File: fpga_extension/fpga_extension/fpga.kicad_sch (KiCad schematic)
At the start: 50 parts, among them U2 t20f169

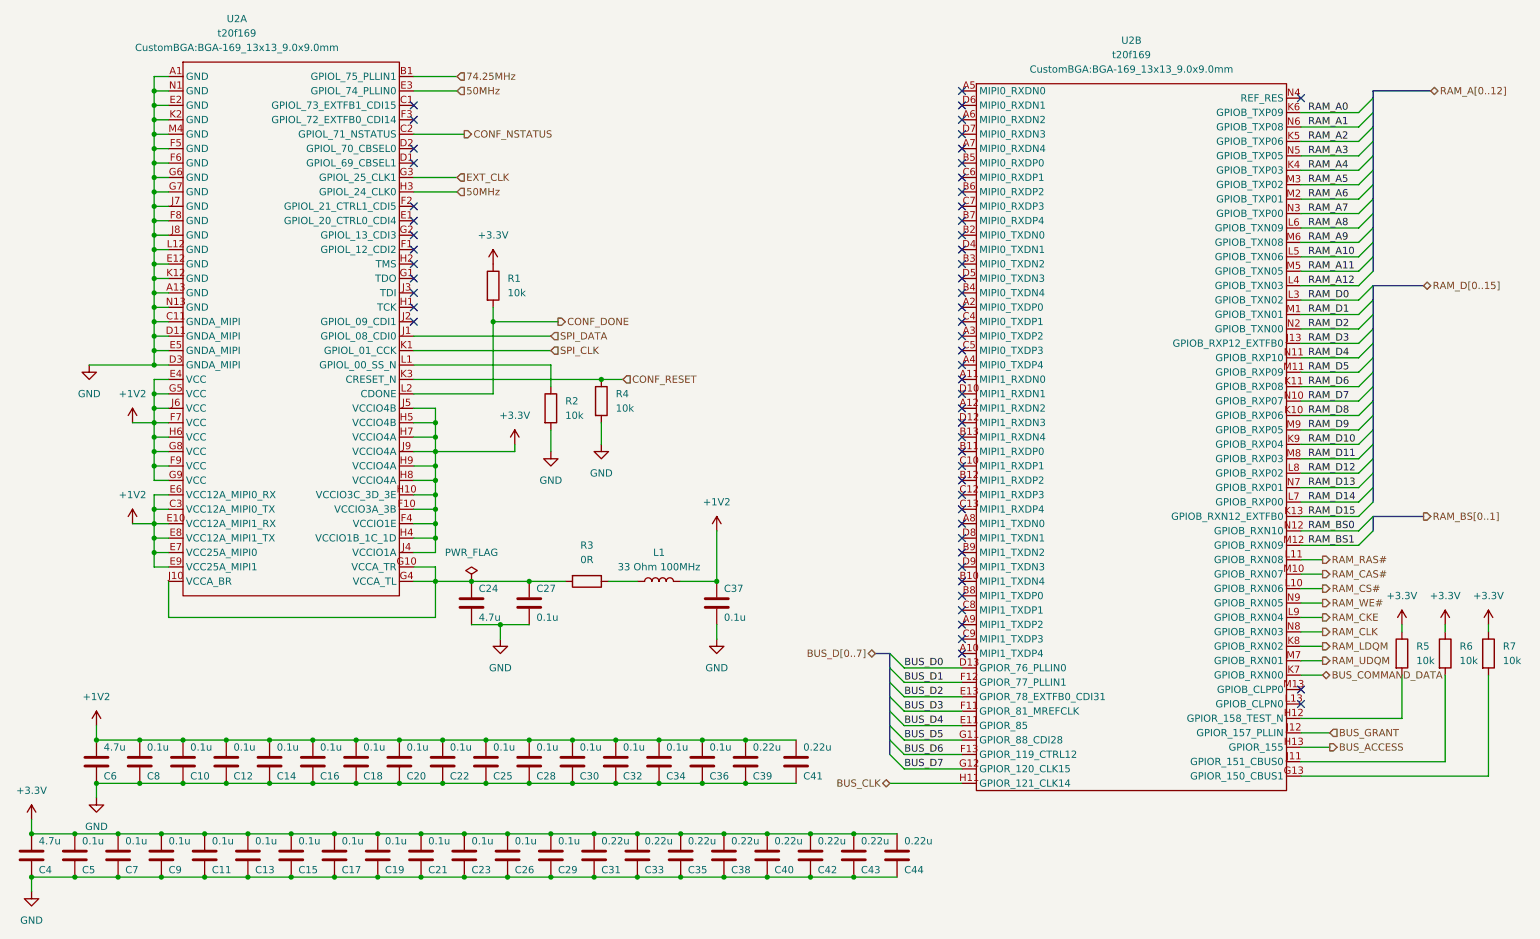
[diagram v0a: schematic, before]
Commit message: working on new version of fpga extension with Lattice FPGA
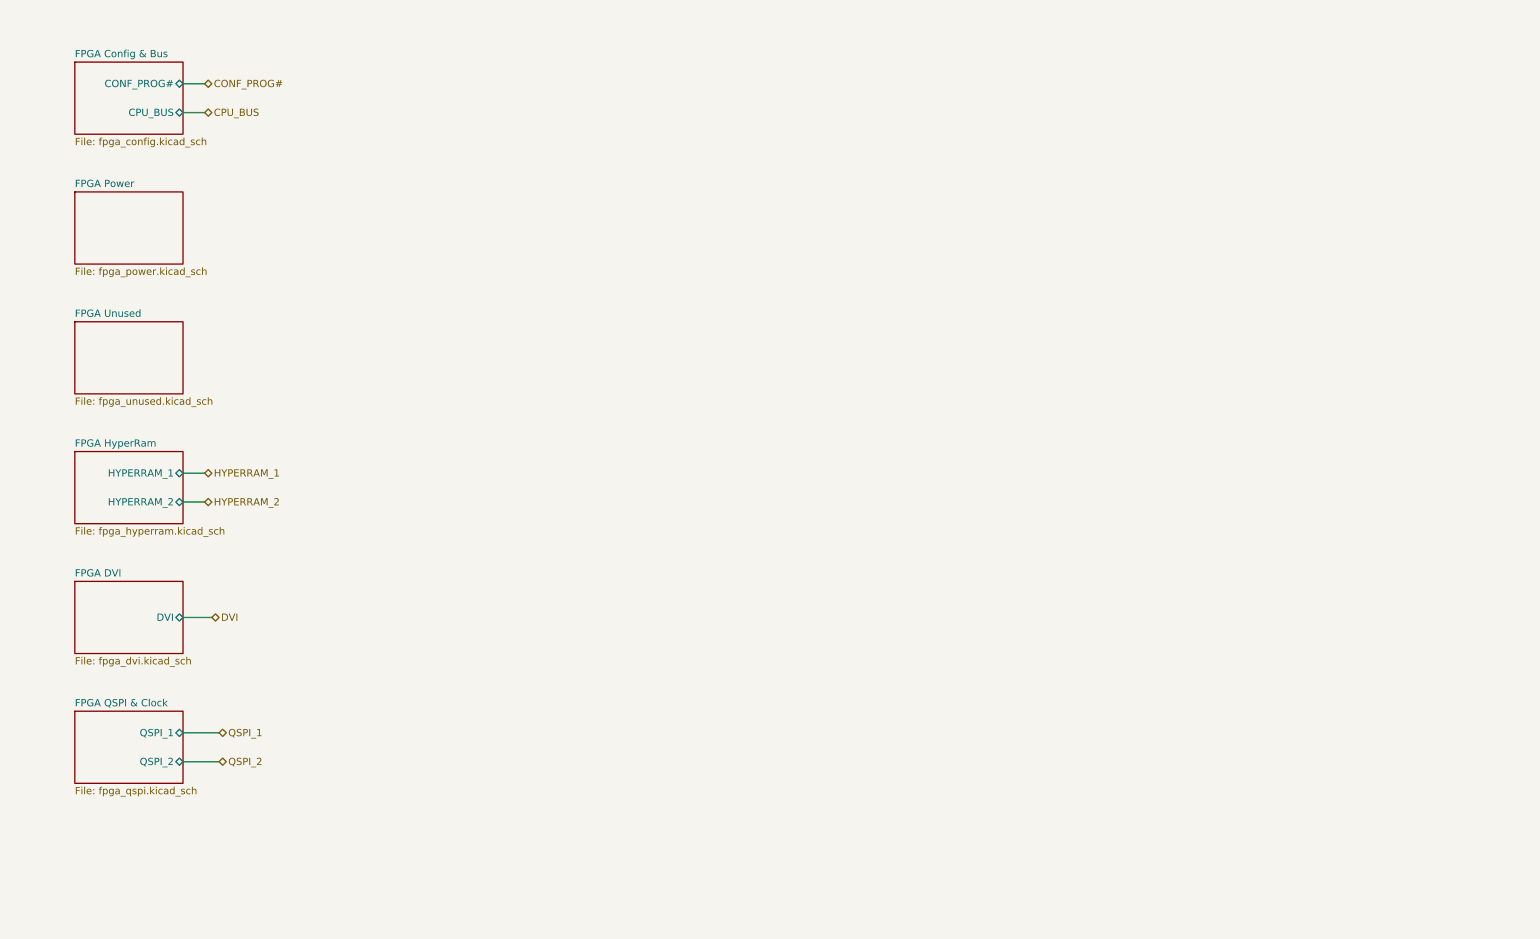
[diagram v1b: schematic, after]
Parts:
- removed C10, C11, C12, C13, C14, C15, C16, C17, C18, C19, C20, C21, C22, C23, C25, C26, C27, C28, C29, C30, C32, C34, C36, C37, C5, C7, C8, C9: 0.1u, Capacitor_SMD:C_0201_0603Metric_Pad0.64x0.40mm_HandSolder, symbol Device:C
- removed C24: 4.7u, Capacitor_SMD:C_0201_0603Metric_Pad0.64x0.40mm_HandSolder, symbol Device:C
- removed C31, C33, C35, C38, C39, C40, C41, C42, C43, C44: 0.22u, Capacitor_SMD:C_0201_0603Metric_Pad0.64x0.40mm_HandSolder, symbol Device:C
- removed C4, C6: 4.7u, Capacitor_SMD:C_0402_1005Metric_Pad0.74x0.62mm_HandSolder, symbol Device:C
- removed L1: 33 Ohm 100MHz, Inductor_SMD:L_0402_1005Metric_Pad0.77x0.64mm_HandSolder, symbol Device:L
- removed R1, R2, R4, R5, R6, R7: 10k, Resistor_SMD:R_0603_1608Metric_Pad0.98x0.95mm_HandSolder, symbol Device:R
- removed R3: 0R, Resistor_SMD:R_0201_0603Metric_Pad0.64x0.40mm_HandSolder, symbol Device:R
- removed U2: t20f169, CustomBGA:BGA-169_13x13_9.0x9.0mm, symbol FPGA_Efinix:t20f169
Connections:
- no-connect marks 56 -> 0
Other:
- added sheet FPGA Config & Bus (fpga_config.kicad_sch)
- added sheet FPGA DVI (fpga_dvi.kicad_sch)
- added sheet FPGA HyperRam (fpga_hyperram.kicad_sch)
- added sheet FPGA Power (fpga_power.kicad_sch)
- added sheet FPGA QSPI & Clock (fpga_qspi.kicad_sch)
- added sheet FPGA Unused (fpga_unused.kicad_sch)

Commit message: refactored mainboard schematic
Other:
- sheet FPGA Config & Bus renamed FPGA Config, Bus & Clock
- sheet FPGA HyperRam renamed FPGA RAM
- removed sheet FPGA DVI
- sheet FPGA Config, Bus & Clock ports: added BUS{IO[0...7] CS#[0..1] INT RE# CLK RWDS}, JTAG{TDO TCK TDI TMS}; removed CONF_PROG#, CPU_BUS
- sheet FPGA QSPI & Clock ports: added QSPI1{CE# SCLK IO[0...3]}, QSPI2{CE# SCLK IO[0...3]}; removed QSPI_1, QSPI_2
- sheet FPGA RAM ports: added none; removed HYPERRAM_1, HYPERRAM_2
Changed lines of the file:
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@@
 (kicad_sch (version 20221004) (generator eeschema)
   (paper "A4")
-  (wire (pts (xy 44.45 29.21) (xy 48.26 29.21))
-    (stroke (width 0) (type default))
-  )
-  (wire (pts (xy 44.45 143.51) (xy 50.8 143.51))
-    (stroke (width 0) (type default))
-  )
-  (wire (pts (xy 44.45 148.59) (xy 50.8 148.59))
-    (stroke (width 0) (type default))
-  )
-  (wire (pts (xy 44.45 102.87) (xy 48.26 102.87))
-    (stroke (width 0) (type default))
-  )
-  (wire (pts (xy 44.45 34.29) (xy 48.26 34.29))
-    (stroke (width 0) (type default))
-  )
-  (wire (pts (xy 44.45 123.19) (xy 49.53 123.19))
-    (stroke (width 0) (type default))
-  )
-  (wire (pts (xy 44.45 97.79) (xy 48.26 97.79))
-    (stroke (width 0) (type default))
-  )
-  (hierarchical_label "QSPI_2" (shape bidirectional) (at 50.8 148.59 0) (fields_autoplaced)
-    (effects (font (size 1.27 1.27)) (justify left))
-  )
-  (hierarchical_label "CONF_PROG#" (shape bidirectional) (at 48.26 29.21 0) (fields_autoplaced)
-    (effects (font (size 1.27 1.27)) (justify left))
-  )
-  (hierarchical_label "HYPERRAM_2" (shape bidirectional) (at 48.26 102.87 0) (fields_autoplaced)
-    (effects (font (size 1.27 1.27)) (justify left))
-  )
-  (hierarchical_label "DVI" (shape bidirectional) (at 49.53 123.19 0) (fields_autoplaced)
-    (effects (font (size 1.27 1.27)) (justify left))
-  )
-  (hierarchical_label "HYPERRAM_1" (shape bidirectional) (at 48.26 97.79 0) (fields_autoplaced)
-    (effects (font (size 1.27 1.27)) (justify left))
-  )
-  (hierarchical_label "QSPI_1" (shape bidirectional) (at 50.8 143.51 0) (fields_autoplaced)
-    (effects (font (size 1.27 1.27)) (justify left))
-  )
-  (hierarchical_label "CPU_BUS" (shape bidirectional) (at 48.26 34.29 0) (fields_autoplaced)
-    (effects (font (size 1.27 1.27)) (justify left))
-  )
   (sheet (at 25.4 48.26) (size 19.05 12.7) (fields_autoplaced)
     (stroke (width 0.1524) (type solid))
@@
     )
   )
-  (sheet (at 25.4 139.7) (size 19.05 12.7) (fields_autoplaced)
+  (sheet (at 25.4 120.65) (size 29.21 12.7) (fields_autoplaced)
     (stroke (width 0.1524) (type solid))
     (fill (color 0 0 0 0.0000))
-    (property "Sheetname" "FPGA QSPI & Clock" (at 25.4 138.9884 0)
+    (property "Sheetname" "FPGA QSPI & Clock" (at 25.4 119.9384 0)
       (effects (font (size 1.27 1.27)) (justify left bottom))
     )
-    (property "Sheetfile" "fpga_qspi.kicad_sch" (at 25.4 152.9846 0)
+    (property "Sheetfile" "fpga_qspi.kicad_sch" (at 25.4 133.9346 0)
       (effects (font (size 1.27 1.27)) (justify left top))
     )
-    (pin "QSPI_1" bidirectional (at 44.45 143.51 0)
+    (pin "QSPI1{CE# SCLK IO[0...3]}" bidirectional (at 54.61 124.46 0)
       (effects (font (size 1.27 1.27)) (justify right))
     )
-    (pin "QSPI_2" bidirectional (at 44.45 148.59 0)
+    (pin "QSPI2{CE# SCLK IO[0...3]}" bidirectional (at 54.61 129.54 0)
       (effects (font (size 1.27 1.27)) (justify right))
     )
@@
     (stroke (width 0.1524) (type solid))
     (fill (color 0 0 0 0.0000))
-    (property "Sheetname" "FPGA HyperRam" (at 25.4 93.2684 0)
+    (property "Sheetname" "FPGA RAM" (at 25.4 93.2684 0)
       (effects (font (size 1.27 1.27)) (justify left bottom))
     )
     (property "Sheetfile" "fpga_hyperram.kicad_sch" (at 25.4 107.2646 0)
       (effects (font (size 1.27 1.27)) (justify left top))
-    )
-    (pin "HYPERRAM_2" bidirectional (at 44.45 102.87 0)
-      (effects (font (size 1.27 1.27)) (justify right))
-    )
-    (pin "HYPERRAM_1" bidirectional (at 44.45 97.79 0)
-      (effects (font (size 1.27 1.27)) (justify right))
     )
   )
@@
     )
   )
-  (sheet (at 25.4 116.84) (size 19.05 12.7) (fields_autoplaced)
+  (sheet (at 25.4 25.4) (size 49.53 16.51) (fields_autoplaced)
     (stroke (width 0.1524) (type solid))
     (fill (color 0 0 0 0.0000))
-    (property "Sheetname" "FPGA DVI" (at 25.4 116.1284 0)
+    (property "Sheetname" "FPGA Config, Bus & Clock" (at 25.4 24.6884 0)
       (effects (font (size 1.27 1.27)) (justify left bottom))
     )
-    (property "Sheetfile" "fpga_dvi.kicad_sch" (at 25.4 130.1246 0)
+    (property "Sheetfile" "fpga_config.kicad_sch" (at 25.4 42.4946 0)
       (effects (font (size 1.27 1.27)) (justify left top))
     )
-    (pin "DVI" bidirectional (at 44.45 123.19 0)
+    (pin "BUS{IO[0...7] CS#[0..1] INT RE# CLK RWDS}" bidirectional (at 74.93 35.56 0)
       (effects (font (size 1.27 1.27)) (justify right))
     )
-  )
-  (sheet (at 25.4 25.4) (size 19.05 12.7) (fields_autoplaced)
-    (stroke (width 0.1524) (type solid))
-    (fill (color 0 0 0 0.0000))
-    (property "Sheetname" "FPGA Config & Bus" (at 25.4 24.6884 0)
-      (effects (font (size 1.27 1.27)) (justify left bottom))
-    )
-    (property "Sheetfile" "fpga_config.kicad_sch" (at 25.4 38.6846 0)
-      (effects (font (size 1.27 1.27)) (justify left top))
-    )
-    (pin "CONF_PROG#" bidirectional (at 44.45 29.21 0)
+    (pin "JTAG{TDO TCK TDI TMS}" bidirectional (at 74.93 30.48 0)
       (effects (font (size 1.27 1.27)) (justify right))
     )
-    (pin "CPU_BUS" bidirectional (at 44.45 34.29 0)
-      (effects (font (size 1.27 1.27)) (justify right))
-    )
